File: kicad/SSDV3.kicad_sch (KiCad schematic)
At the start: 12 parts, among them J7 SolderPad_1x02, J8 SolderPad_1x03

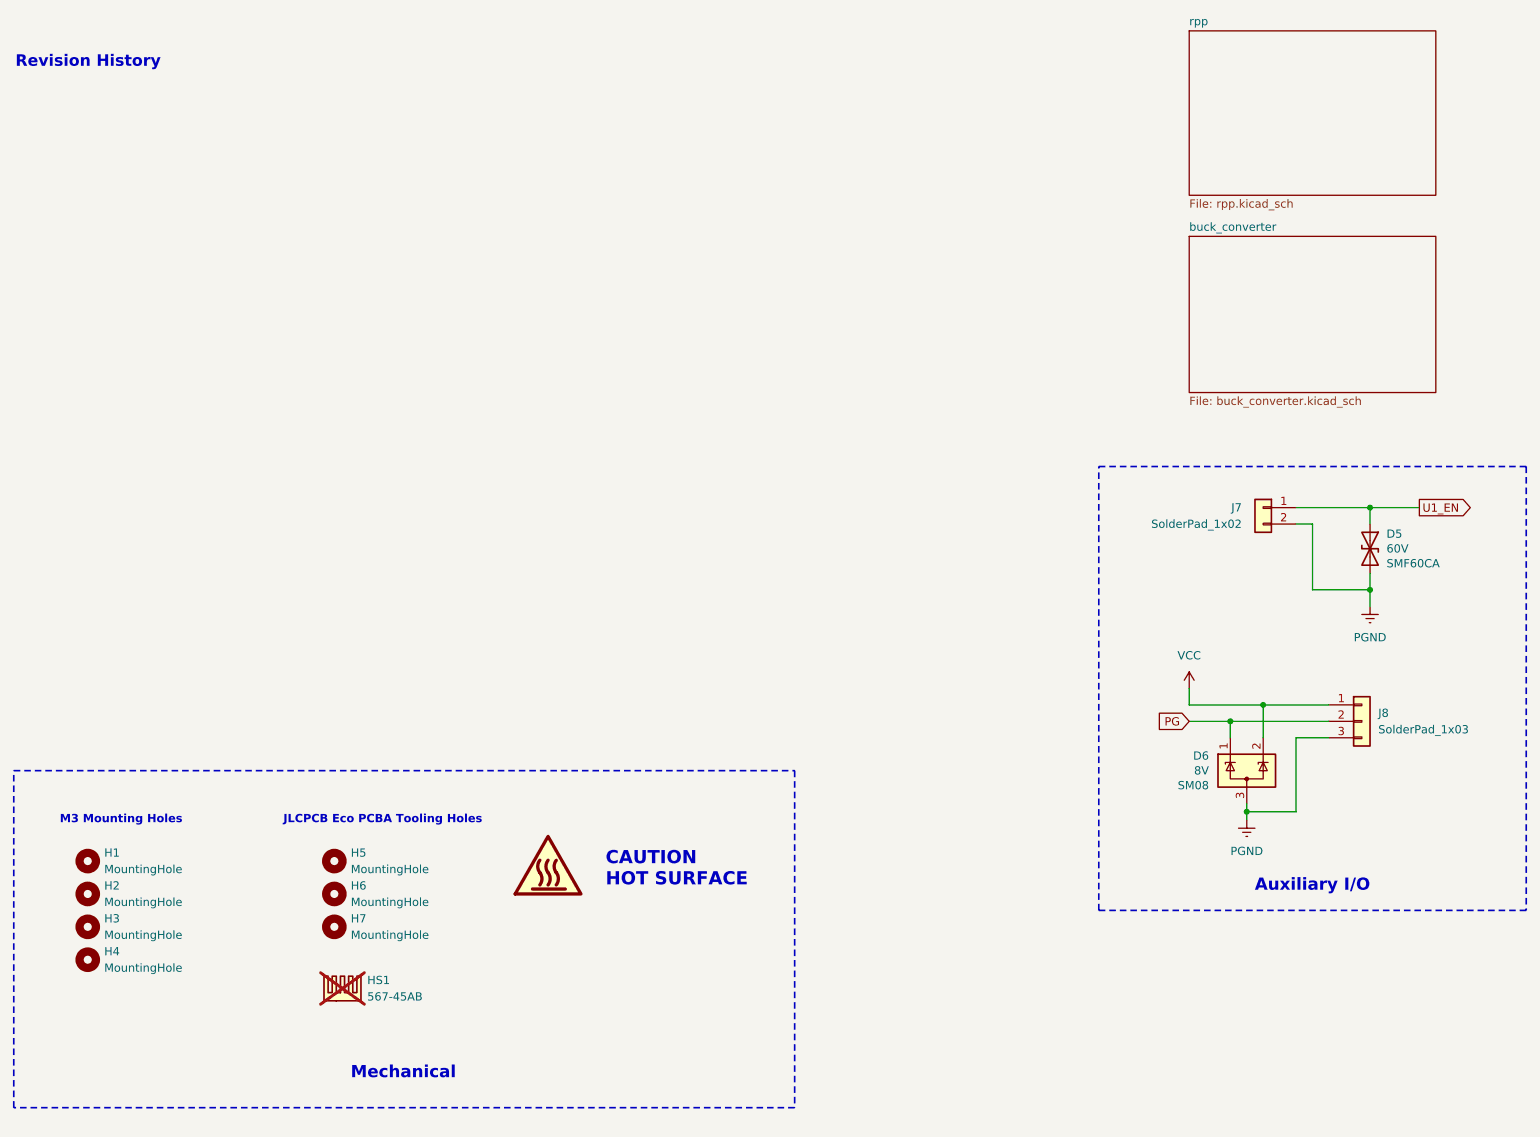
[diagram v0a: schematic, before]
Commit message: Adjusted licensing for club
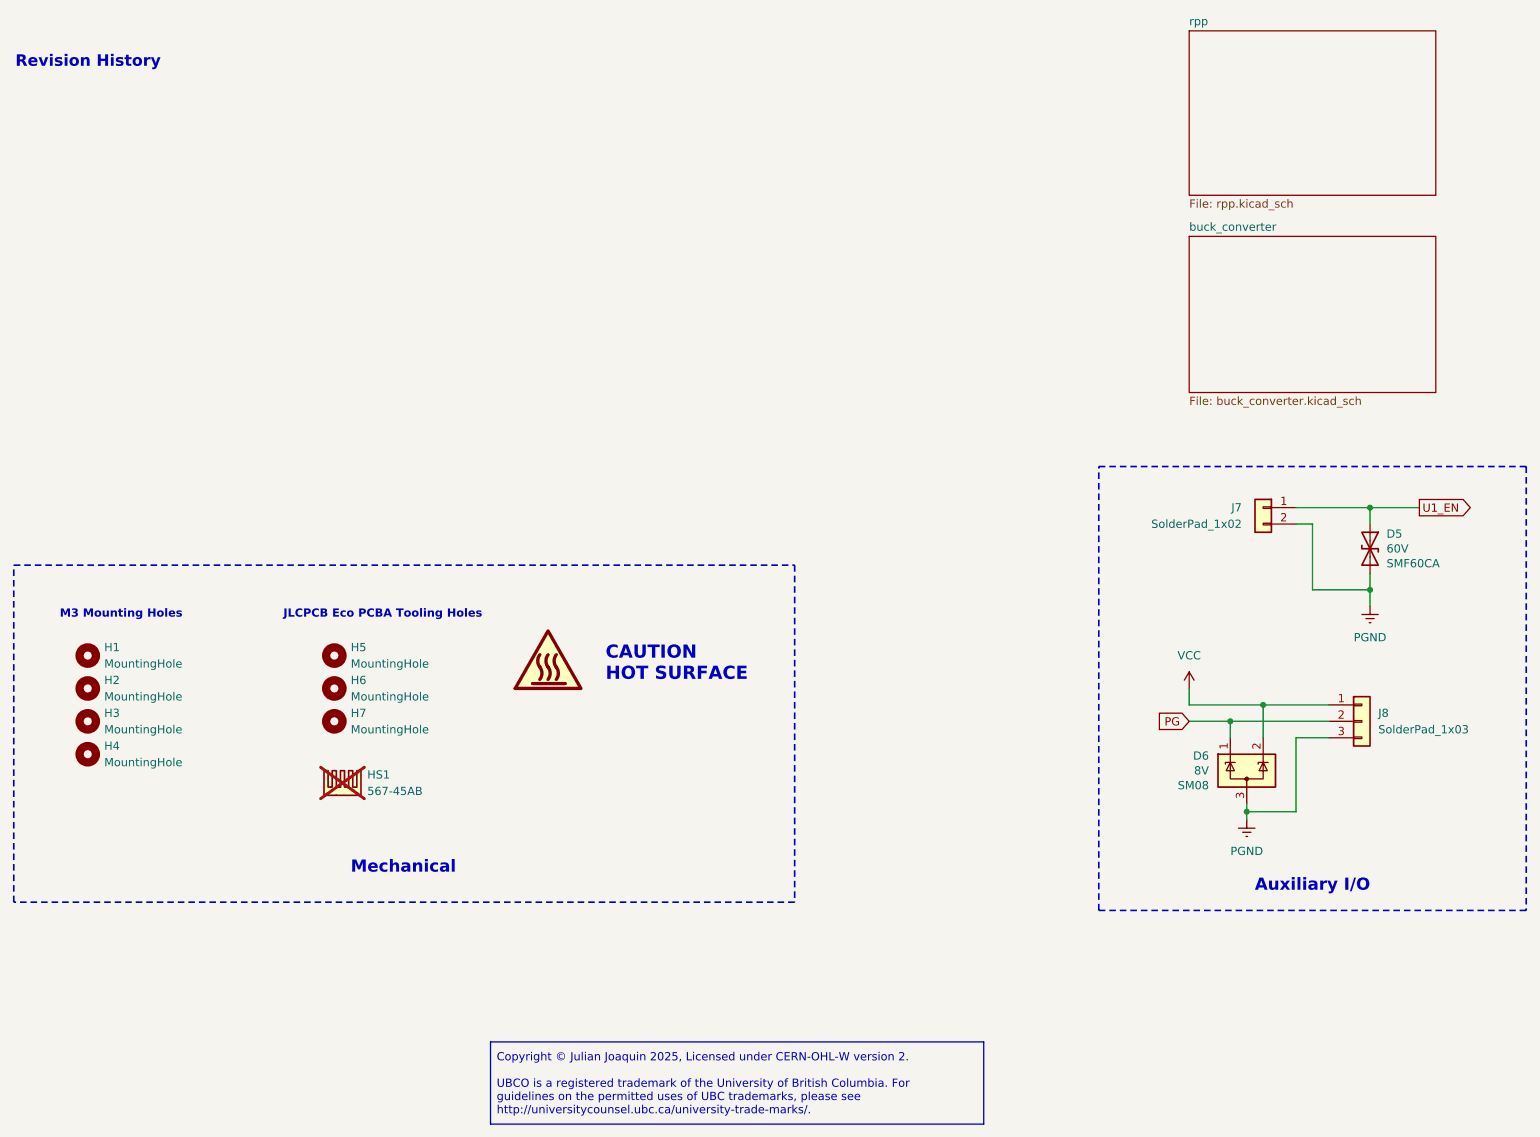
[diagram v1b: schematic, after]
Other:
- company: Author: Julian Joaquin -> UBCO Aerospace Club
- moved on the sheet: H1, H2, H3, H4, H5, H6, H7, HS1

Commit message: Added heatsink footprint
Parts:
- removed H1, H2, H3, H4: MountingHole, MountingHole:MountingHole_3.2mm_M3_ISO7380, symbol Mechanical:MountingHole
- HS1: value 567-45AB -> 241802B92200G; footprint (none) -> Heatsink_JJ:24180xB9x200G; Manufacturer Wakefield-Vette -> Aavid; now fitted
